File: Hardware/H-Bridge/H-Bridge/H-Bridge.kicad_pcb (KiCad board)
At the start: 2 copper layers, 74.4 x 46 mm, 20 parts, among them Q1 FDS8896, Q2 FDS8896, Q3 FDS8896, Q4 FDS8896, U1 IRS2005S, U2 IRS2005S, U3 Teensy4.1_DEV-16771

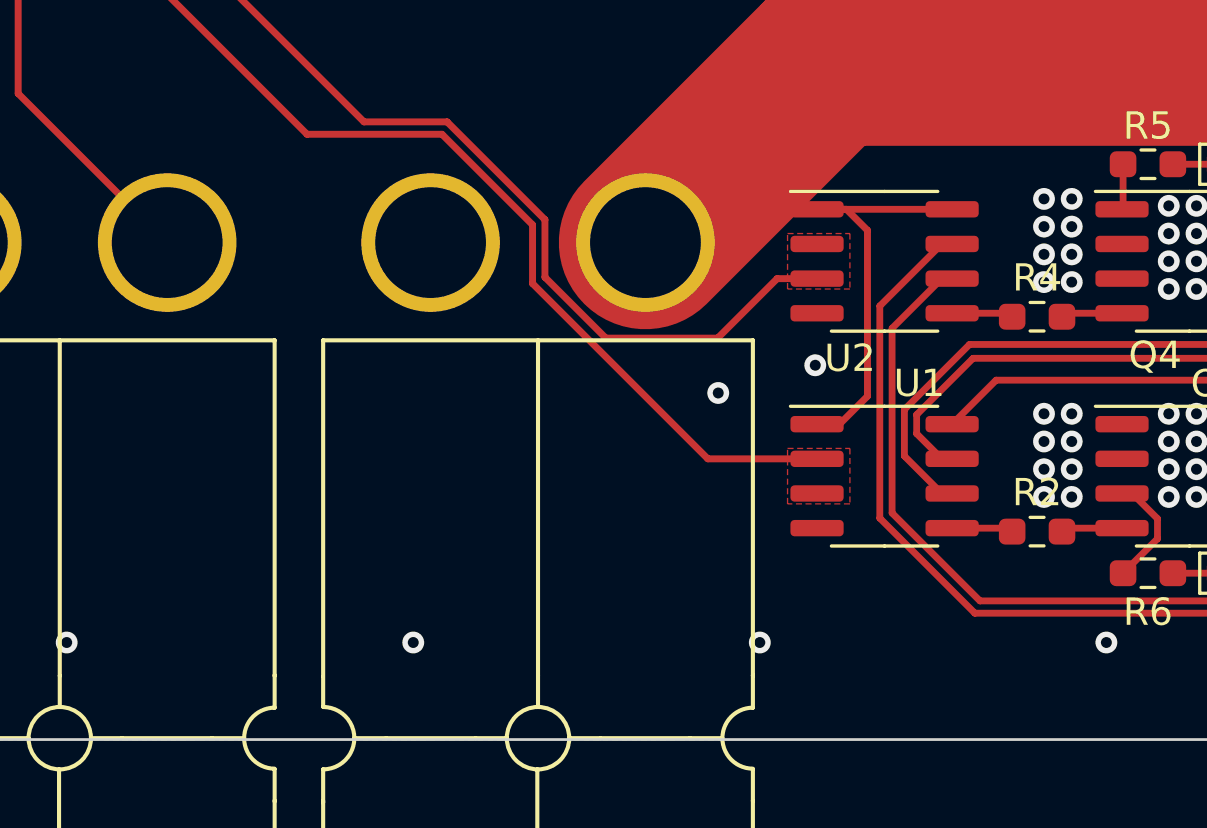
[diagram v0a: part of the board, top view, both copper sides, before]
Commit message: Fixed organization, added BOM
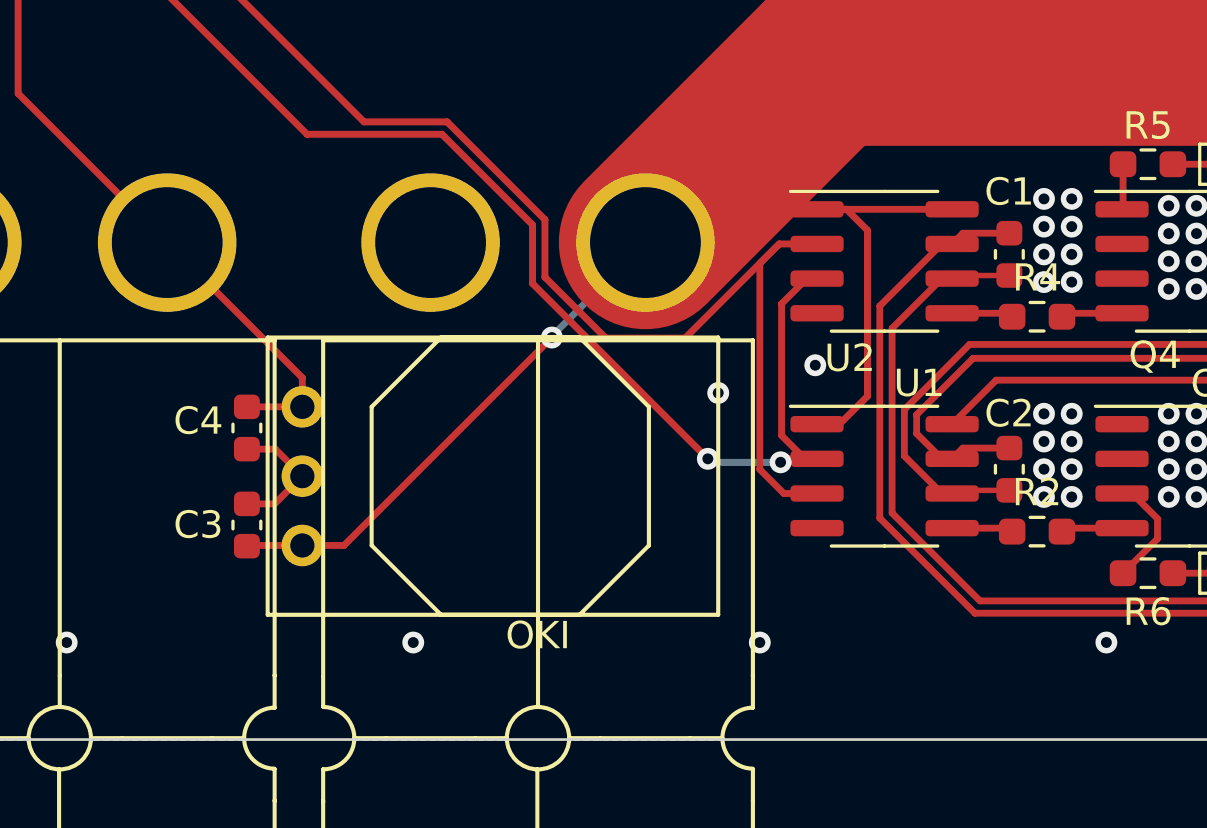
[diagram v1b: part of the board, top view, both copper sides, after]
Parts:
- added C1: 0.1u, Capacitor_SMD:C_0603_1608Metric, F.Cu at (98.0, 74.7)
- added C2: 0.1u, Capacitor_SMD:C_0603_1608Metric, F.Cu at (98.0, 82.5)
- added C3: 10u, Capacitor_SMD:C_0603_1608Metric, F.Cu at (70.1, 84.6)
- added C4: 10u, Capacitor_SMD:C_0603_1608Metric, F.Cu at (70.1, 81.0)
- added U4: OKI, MRDT_Devices:OKI_Horizontal, F.Cu at (72.1, 85.3)
- Q1, Q2, Q3, Q4: value FDS8896 -> SI4156DY
- R5, R6: value 100 -> 1K
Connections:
- R2 pad 2: Net-(Q2-Pad4) -> Net-(Q4-Pad4)
- R4 pad 2: Net-(Q4-Pad4) -> Net-(Q2-Pad4)
- U1 pad 3: FWD_PWM -> RVS_PWM
- U2 pad 3: RVS_PWM -> FWD_PWM
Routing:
- net +12V: track 96.2 -> 115.4 mm, vias 0 -> 1
- net RVS_PWM: track 31.3 -> 42.9 mm
- net +5V: track 28.9 -> 39.0 mm
- net FWD_PWM: track 34.8 -> 43.1 mm, vias 0 -> 2
- net GND: track 5.87 -> 10.8 mm
- net Net-(R3-Pad1): track 34.8 -> 37.0 mm
- net Net-(R1-Pad1): track 23.0 -> 25.2 mm
- net /M-: track 27.1 -> 29.3 mm
- net /M+: track 20.2 -> 22.4 mm
- removed copper zone on F.Cu, net FWD_PWM
- removed copper zone on F.Cu, net RVS_PWM

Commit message: The whole gosh dang schematic
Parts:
- moved C1 7.87 mm to (98.0, 82.5)
- moved C2 7.87 mm to (98.0, 74.7)
- moved R2 7.87 mm to (99.1, 77.0)
- moved R4 7.87 mm to (99.1, 84.8)
- moved U1 7.87 mm to (93.5, 74.9)
- moved U2 7.87 mm to (93.5, 82.8)
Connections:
- C1 pad 1: Net-(R3-Pad1) -> +12V
- C2 pad 1: Net-(R1-Pad1) -> +12V
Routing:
- net +12V: track 115.4 -> 99.3 mm
- net Net-(R3-Pad1): track 37.0 -> 26.4 mm
- net /M-: track 29.3 -> 20.9 mm
- net FWD_PWM: track 43.1 -> 47.3 mm
- net RVS_PWM: track 42.9 -> 39.0 mm
- net /M+: track 22.4 -> 19.9 mm

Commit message: Actually Saved this time
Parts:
- Conn1, Conn2, Conn3: footprint MRDT_Connectors:Anderson_2_Horizontal_Side_by_Side -> MRDT_Connectors:Square_Anderson_2_H_Side_By_Side
- moved Conn1 0.79 mm to (76.2, 73.9)
- moved Conn3 0.67 mm to (111.4, 74.4)
- moved Conn2 0.52 mm to (58.9, 73.9)

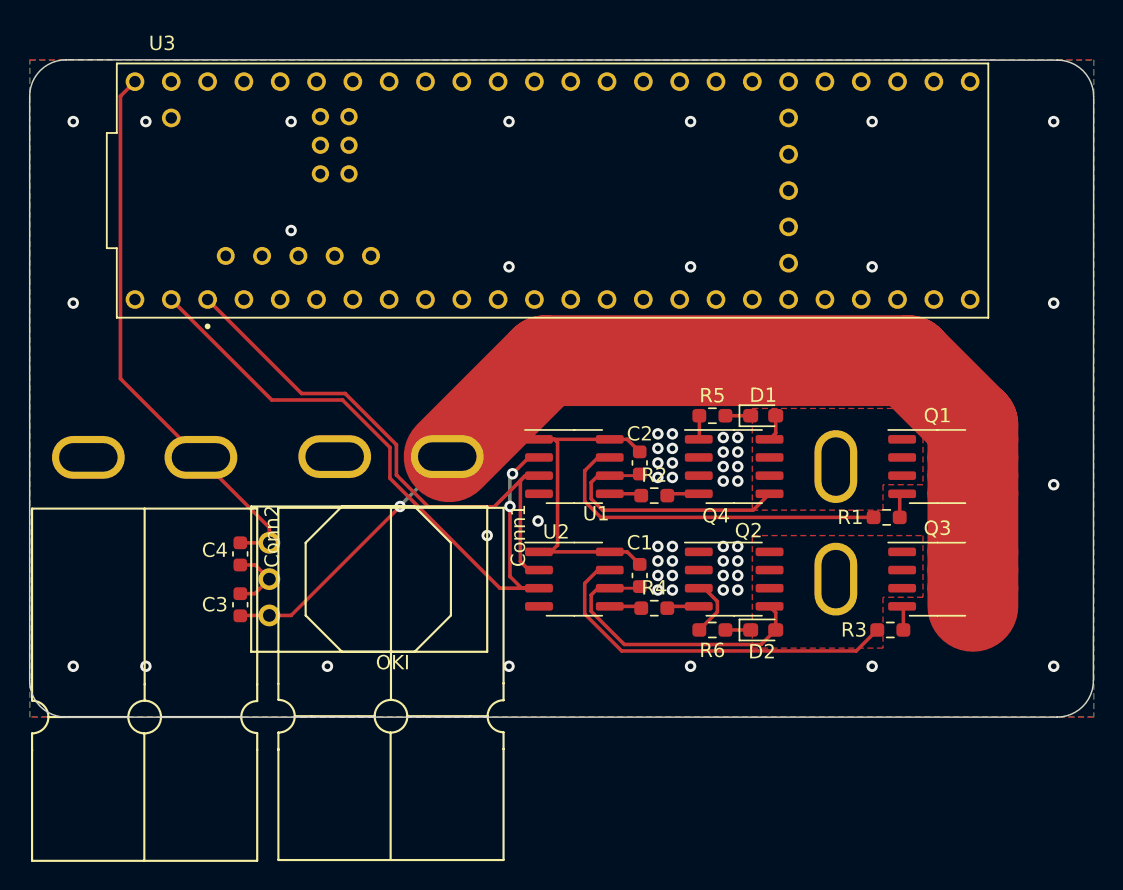
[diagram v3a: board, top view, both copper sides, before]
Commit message: PDR Changes to H-Bridge and Layout
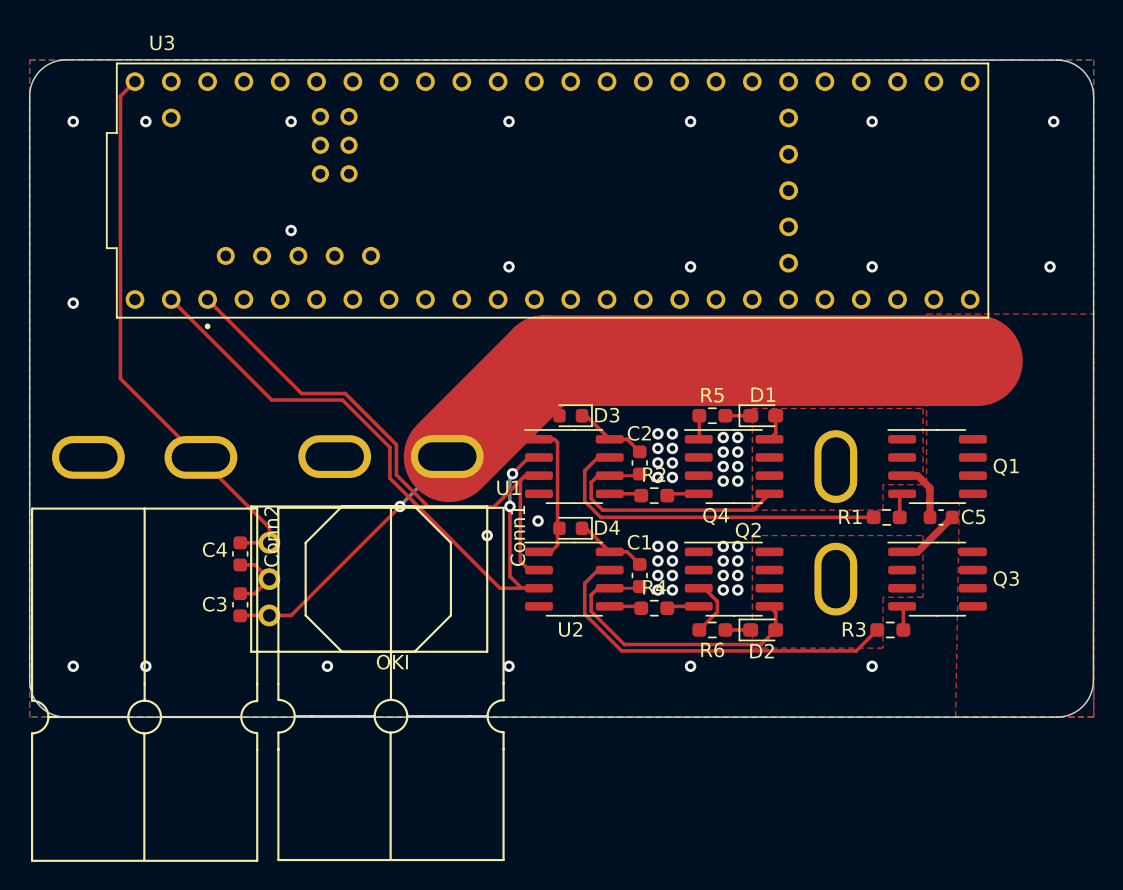
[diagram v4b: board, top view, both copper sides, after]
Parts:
- added C5: 10u, Capacitor_SMD:C_0603_1608Metric, F.Cu at (119.1, 78.5)
- added D3: D_Small, Diode_SMD:D_0603_1608Metric, F.Cu at (93.2, 71.4)
- added D4: D_Small, Diode_SMD:D_0603_1608Metric, F.Cu at (93.2, 79.2)
- D1, D2: value BLUE -> Pink
- R5, R6: value 1K -> 500
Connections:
- C1 pad 1: +12V -> Net-(C1-Pad1)
- C2 pad 1: +12V -> Net-(C2-Pad1)
- C4 pad 1: +5V -> +3V3
- U1 pad 8: +12V -> Net-(C2-Pad1)
- U2 pad 8: +12V -> Net-(C1-Pad1)
- U3 pad VIN: +5V -> +3V3
- U4 pad 3: +5V -> +3V3
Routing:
- net +5V: track 39.0 -> 0.00 mm
- net +3V3: track 0.00 -> 39.0 mm
- net +12V: track 99.3 -> 69.0 mm
- net Net-(C1-Pad1): track 0.00 -> 5.09 mm
- net Net-(C2-Pad1): track 0.00 -> 5.09 mm
- net /M-: track 20.9 -> 25.4 mm
- net /M+: track 19.9 -> 24.3 mm
- net GND: vias 55 -> 53
- added copper zone on F.Cu, net +12V

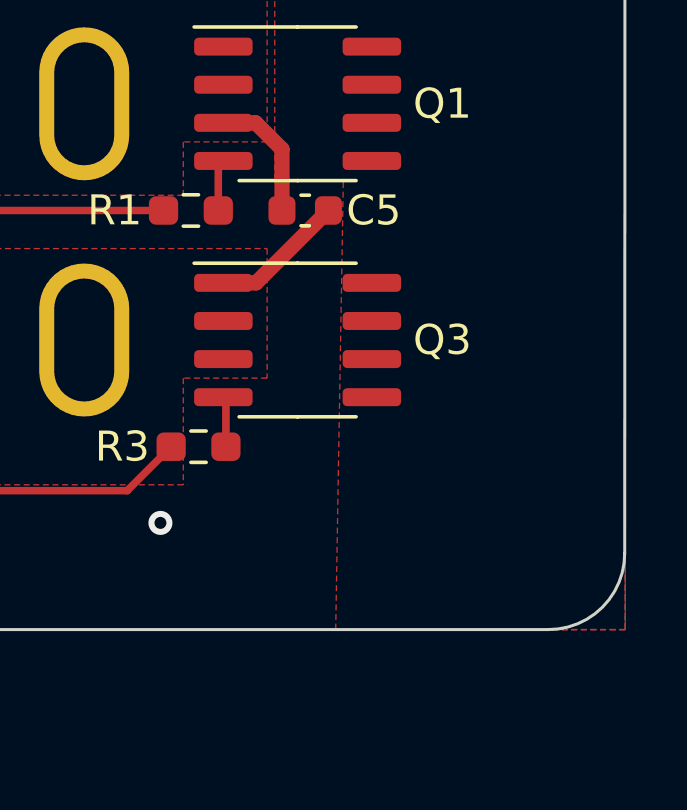
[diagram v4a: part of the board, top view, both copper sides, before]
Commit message: Added Unconnected Flags to H-Bridge
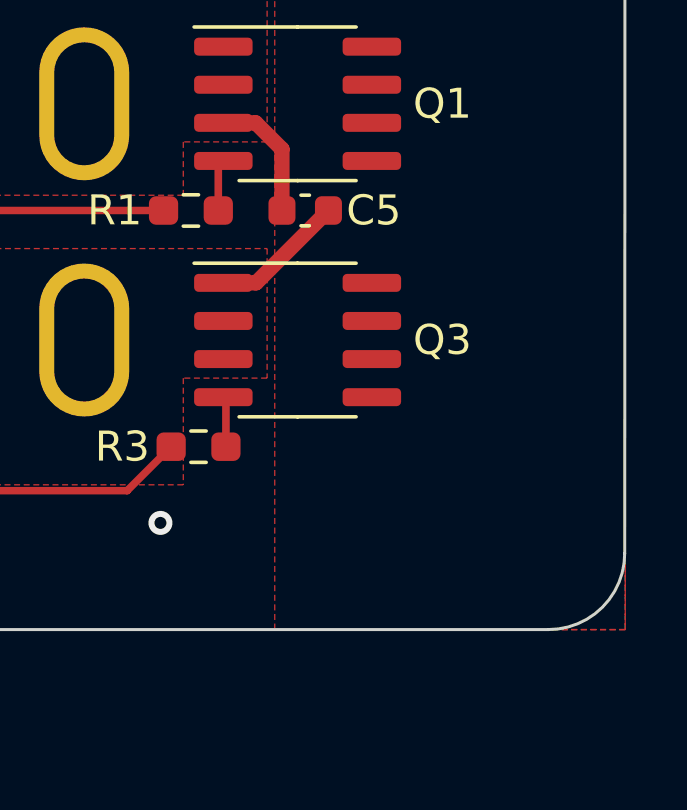
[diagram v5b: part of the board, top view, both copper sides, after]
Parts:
- moved G*** 15.5 mm to (93.5, 65.0)
- moved G*** 2.19 mm to (64.3, 83.0)
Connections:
- Conn2 pad 2: +5V -> +3V3
- U3 pad 3.3V_1: Net-(U3-Pad3.3V_1) -> unconnected-(U3-Pad3.3V_1)
- U3 pad 3.3V_2: Net-(U3-Pad3.3V_1) -> unconnected-(U3-Pad3.3V_1)
- U3 pad 3.3V_3: Net-(U3-Pad3.3V_1) -> unconnected-(U3-Pad3.3V_1)
- U3 pad USB_GND1: GND -> unconnected-(U3-PadUSB_GND1)
- U3 pad USB_GND2: GND -> unconnected-(U3-PadUSB_GND1)
